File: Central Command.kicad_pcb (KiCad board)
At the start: 4 copper layers, 50.8 x 50.8 mm, 54 parts, among them P101 CONN_01X10, P102 CONN_01X10, P103 CONN_01X04, P104 CONN_01X02, P105 CONN_01X04, P106 CONN_01X02, P201 CONN_01X06, P202 CONN_01X04, P203 CONN_01X04, P204 CONN_01X03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

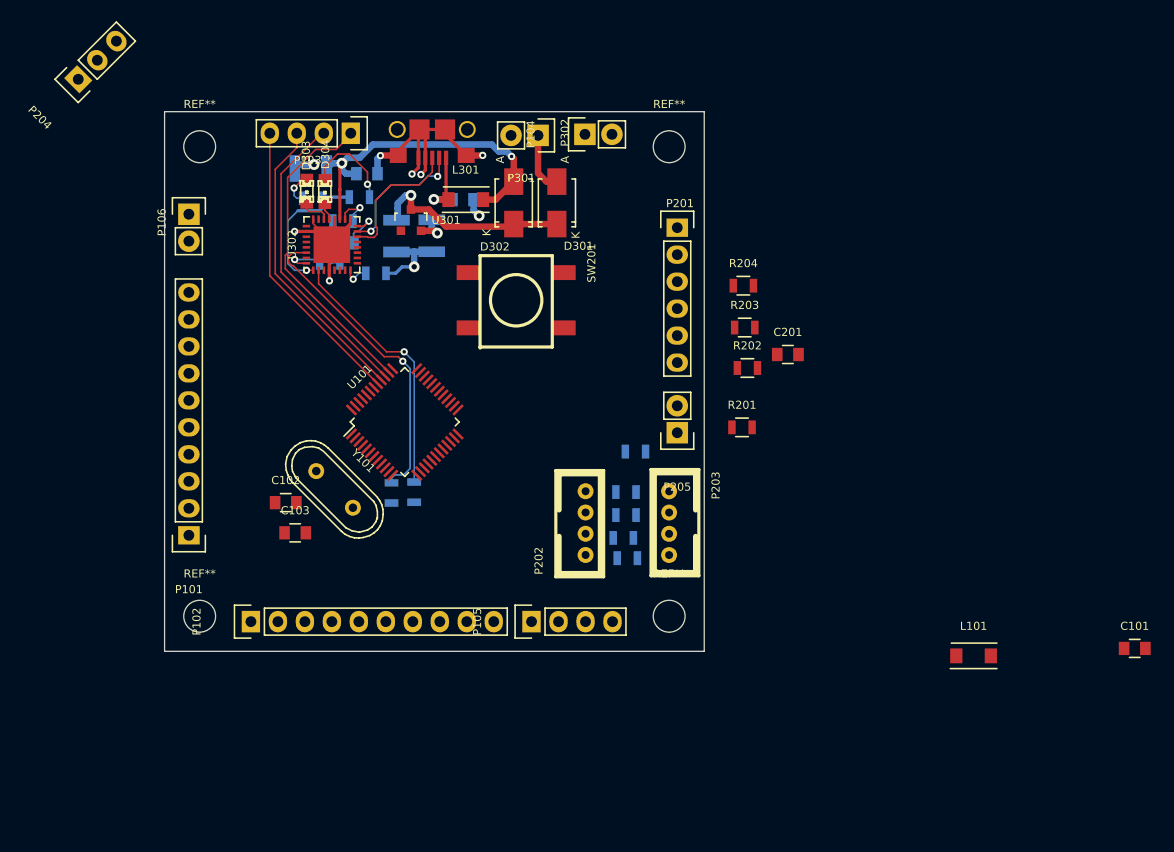
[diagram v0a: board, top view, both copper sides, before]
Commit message: Swapped two connectors and routed the bottom connector
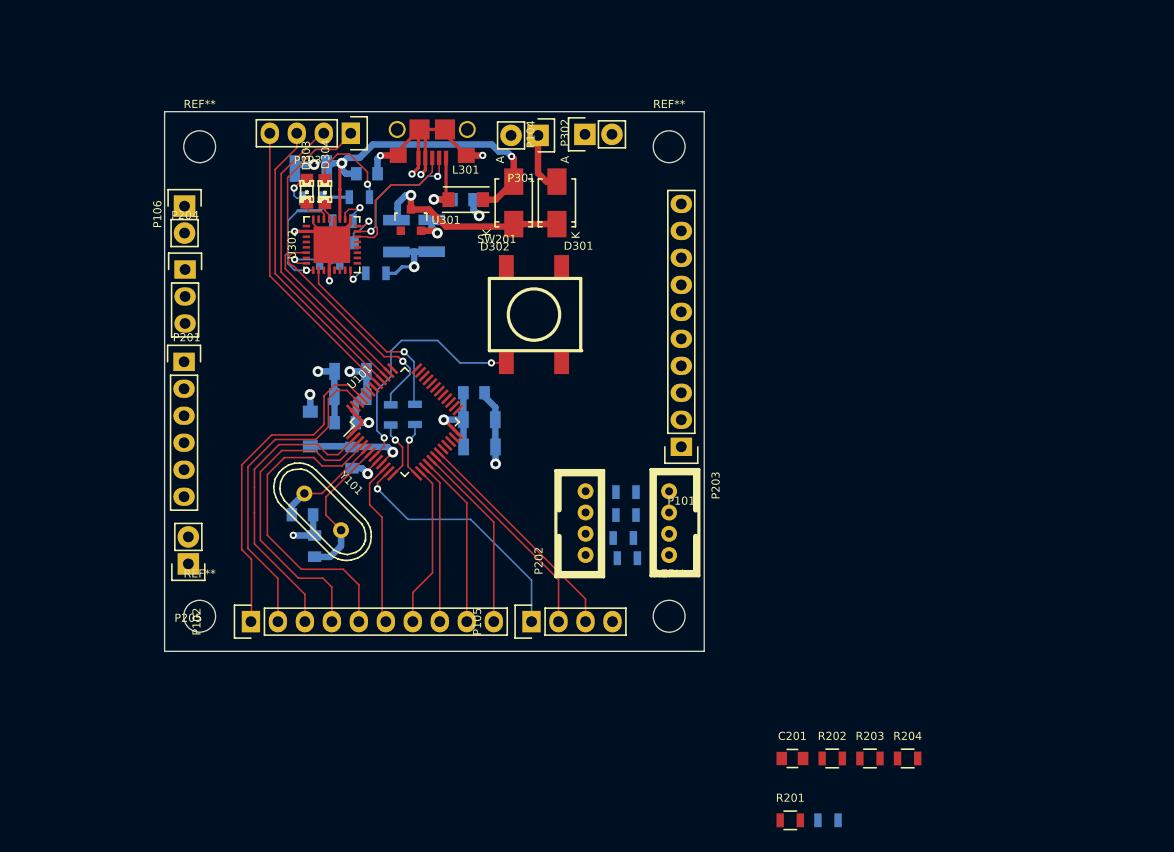
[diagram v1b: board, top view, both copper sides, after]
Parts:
- added C104: .1U, Capacitors_SMD:C_0805, B.Cu at (130.7, 102.7)
- added C105: 1U, Capacitors_SMD:C_1206, B.Cu at (131.3, 107.8)
- added C106: 10U, Capacitors_SMD:C_1206, B.Cu at (131.2, 105.2)
- added C107: .1U, Capacitors_SMD:C_0805, B.Cu at (118.6, 105.5)
- added C108: 1U, Capacitors_SMD:C_1206, B.Cu at (119.1, 103.0)
- added C109: 10U, Capacitors_SMD:C_1206, B.Cu at (119.1, 100.6)
- C101, C102, C103, L101: moved to B.Cu
- moved C101 75.9 mm to (119.2, 108.8), turned to 270 degrees
- moved L101 66.0 mm to (115.3, 106.1), turned to 270 degrees
- moved P201 48.1 mm to (103.4, 99.7)
- moved P205 47.7 mm to (103.8, 118.8)
- moved R204 47.1 mm to (171.5, 137.1)
- moved P101 47.1 mm to (150.2, 107.7)
- moved R203 42.2 mm to (168.0, 137.1)
- moved R205 39.2 mm to (164.0, 142.9)
- moved C201 38.0 mm to (160.7, 137.1)
- moved R202 37.6 mm to (164.4, 137.1)
- moved R201 37.3 mm to (160.5, 142.9)
- moved P204 20.5 mm to (103.5, 91.1), turned to 0 degrees
- moved R302 7.34 mm to (122.9, 104.7)
- moved R303 7.32 mm to (125.2, 104.7)
- moved Y101 2.39 mm to (116.5, 113.9)
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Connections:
- net Net-(C101-Pad1) renamed /VDDA
- P101 pad 10: Net-(P101-Pad10) -> /PA10
- P101 pad 8: Net-(P101-Pad8) -> /Comm/MCO
- P101 pad 9: Net-(P101-Pad9) -> /PA9
- P102 pad 1: Net-(P102-Pad1) -> /PB8
- P102 pad 2: Net-(P102-Pad2) -> /PB9
- P102 pad 4: /PB9 -> Net-(P102-Pad4)
- P102 pad 5: /Comm/MCO -> Net-(P102-Pad5)
- U101 pad 2: Net-(P102-Pad1) -> Net-(P102-Pad3)
- U101 pad 20: Net-(P101-Pad3) -> Net-(P101-Pad1)
- U101 pad 21: Net-(P101-Pad5) -> Net-(P101-Pad2)
- U101 pad 22: Net-(P101-Pad6) -> Net-(P101-Pad3)
- U101 pad 25: Net-(P101-Pad7) -> Net-(P101-Pad4)
- U101 pad 26: Net-(P101-Pad8) -> Net-(P101-Pad5)
- U101 pad 27: Net-(P101-Pad9) -> Net-(P101-Pad6)
- U101 pad 28: Net-(P101-Pad10) -> Net-(P101-Pad7)
- U101 pad 3: Net-(P102-Pad2) -> Net-(P102-Pad4)
- U101 pad 30: Net-(P101-Pad1) -> /PA9
- U101 pad 31: Net-(P101-Pad2) -> /PA10
- U101 pad 4: Net-(P102-Pad3) -> Net-(P102-Pad5)
- U101 pad 45: Net-(P101-Pad4) -> /PB8
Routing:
- net /PB8: track 0.00 -> 31.8 mm
- net /PB9: track 0.00 -> 31.2 mm
- net Net-(P102-Pad5): track 0.00 -> 30.5 mm
- net Net-(P102-Pad4): track 0.00 -> 29.5 mm
- net Net-(P102-Pad3): track 0.00 -> 27.8 mm
- net /ADC_IN1: track 0.00 -> 24.0 mm, vias 0 -> 1
- net /Comm/NRST: track 0.00 -> 23.3 mm, vias 0 -> 2
- net /Comm/PWR: track 3.10 -> 26.3 mm, vias 1 -> 5
- net /ADC_IN9: track 0.00 -> 21.6 mm
- net GND: track 57.3 -> 78.3 mm, vias 9 -> 13
- net /ADC_IN8: track 0.00 -> 20.3 mm
- net Net-(P102-Pad10): track 0.00 -> 17.6 mm
- net Net-(P102-Pad9): track 0.00 -> 16.3 mm
- net Net-(P102-Pad6): track 0.00 -> 15.7 mm
- net Net-(P102-Pad7): track 0.00 -> 15.4 mm
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
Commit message: Removed one header and finished connecting all parts
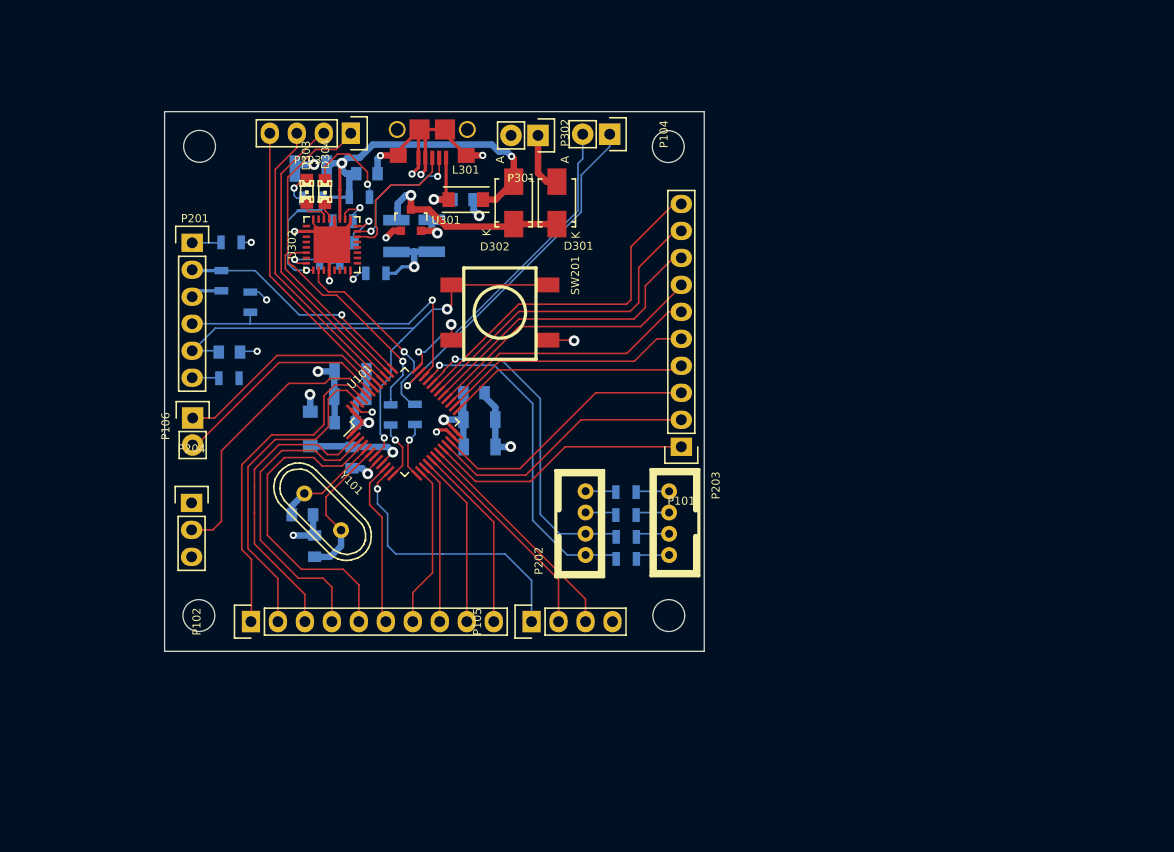
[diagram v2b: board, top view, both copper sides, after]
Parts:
- removed P205: CONN_01X02, Pin_Headers:Pin_Header_Straight_1x02
- removed R205: R, Resistors_SMD:R_0805
- removed the REF** at (149.1, 123.7)
- removed the REF** at (104.9, 123.7)
- removed the REF** at (149.1, 79.5)
- removed the REF** at (104.9, 79.5)
- added REF**: MountingHole_3mm, Mounting_Holes:MountingHole_3mm, F.Cu at (149.0, 79.5)
- added REF**: MountingHole_3mm, Mounting_Holes:MountingHole_3mm, F.Cu at (149.1, 123.6)
- added REF**: MountingHole_3mm, Mounting_Holes:MountingHole_3mm, F.Cu at (104.8, 123.6)
- added REF**: MountingHole_3mm, Mounting_Holes:MountingHole_3mm, F.Cu at (104.9, 79.5)
- C201, R201, R202, R203, R204: moved to B.Cu
- moved R203 77.3 mm to (107.9, 88.5), turned to 180 degrees
- moved R201 73.8 mm to (107.0, 92.1), turned to 270 degrees
- moved R204 73.2 mm to (107.7, 101.3)
- moved R202 69.6 mm to (109.7, 94.1), turned to 270 degrees
- moved C201 65.4 mm to (107.7, 98.8)
- moved P204 22.0 mm to (104.1, 113.0)
- moved P106 20.0 mm to (104.2, 105.0)
- moved P201 11.2 mm to (104.2, 88.5)
- moved SW201 3.22 mm to (133.2, 95.1), turned to 90 degrees
- moved P104 2.33 mm to (143.5, 78.3), turned to 270 degrees
- moved R208 0.30 mm to (145.1, 116.2)
- moved R209 0.12 mm to (145.1, 118.3)
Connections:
- net /Comm/MCO renamed /MCO
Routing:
- net /I2C1_SDA: track 0.00 -> 33.3 mm, vias 0 -> 1
- net /PA10: track 0.00 -> 33.2 mm
- net /Comm/SDA: track 0.00 -> 32.5 mm, vias 0 -> 1
- net /Comm/SWIO: track 0.00 -> 32.2 mm, vias 0 -> 1
- net /Comm/SCL: track 0.00 -> 31.7 mm, vias 0 -> 1
- net /PA9: track 0.00 -> 31.0 mm
- net /Comm/NRST: track 23.3 -> 53.7 mm
- net /I2C1_SCL: track 0.00 -> 29.9 mm, vias 0 -> 1
- net /MCO: track 0.00 -> 29.0 mm
- net /Comm/BOOT0: track 0.00 -> 26.9 mm
- net Net-(P101-Pad7): track 0.00 -> 26.6 mm
- net Net-(P101-Pad3): track 0.00 -> 25.7 mm
- net Net-(P101-Pad2): track 0.00 -> 25.4 mm
- net Net-(P101-Pad6): track 0.00 -> 25.3 mm
- net Net-(P101-Pad1): track 0.00 -> 25.0 mm
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
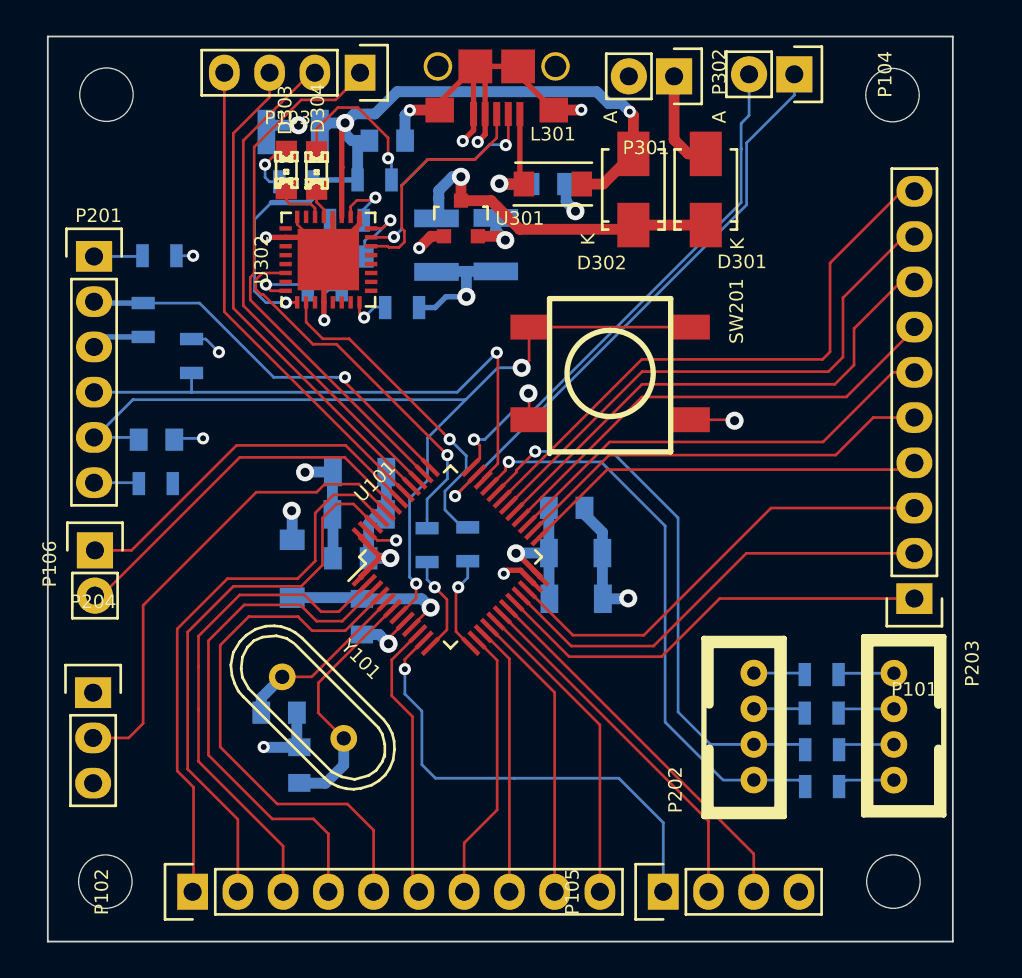
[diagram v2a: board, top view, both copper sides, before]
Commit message: Finished layout including labels and DRC
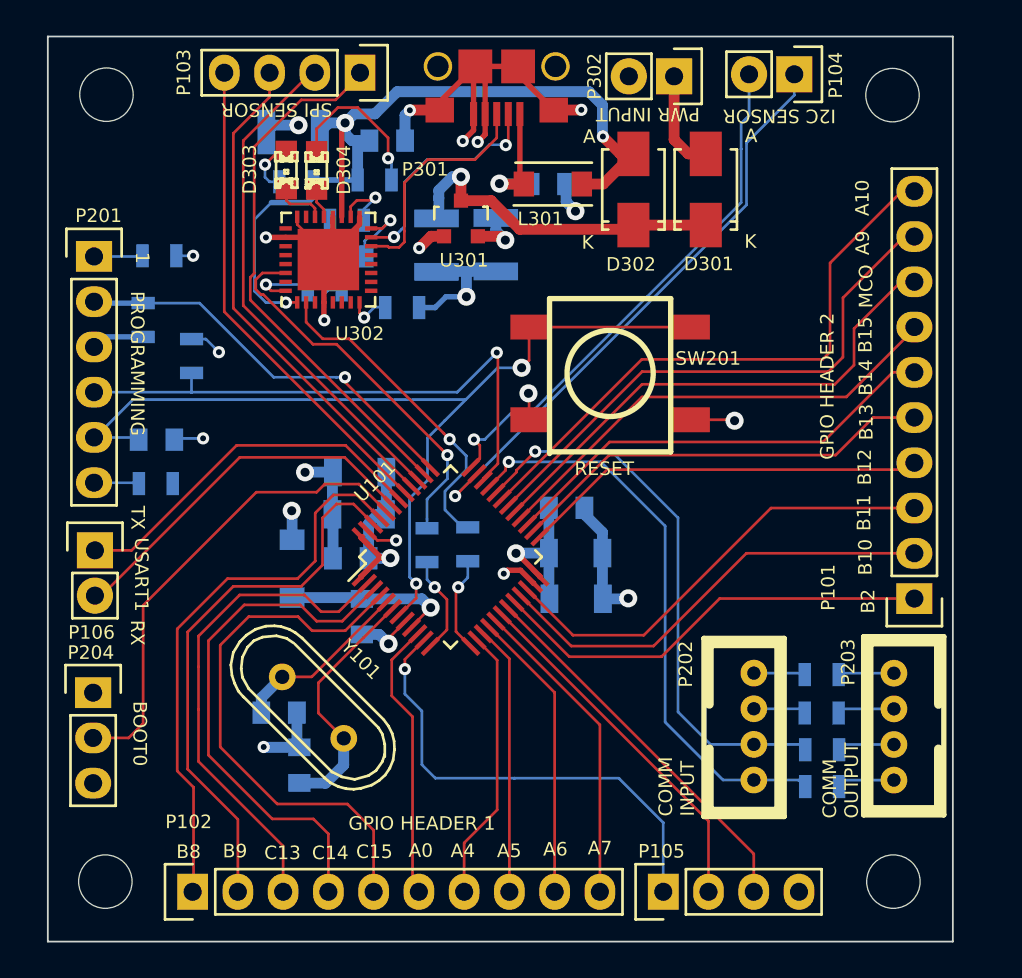
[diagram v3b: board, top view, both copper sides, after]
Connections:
- net Net-(P101-Pad1) renamed /PB2
- net Net-(P101-Pad2) renamed /PB10
- net Net-(P101-Pad3) renamed /PB11
- net Net-(P101-Pad4) renamed /PB12
- net Net-(P101-Pad5) renamed /PB13
- net Net-(P101-Pad6) renamed /PB14
- net Net-(P101-Pad7) renamed /PB15
- net Net-(P102-Pad10) renamed /PA7
- net Net-(P102-Pad3) renamed /PC13
- net Net-(P102-Pad4) renamed /PC14
- net Net-(P102-Pad5) renamed /PC15
- net Net-(P102-Pad6) renamed /PA0
- net Net-(P102-Pad7) renamed /PA4
- net Net-(P102-Pad8) renamed /PA5
- net Net-(P102-Pad9) renamed /PA6
- P301 pad 6: (no net) -> GND
- P301 pad 7: (no net) -> GND
- P301 pad 8: (no net) -> GND
- P301 pad 9: (no net) -> GND
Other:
- board text added: "1"
- board text added: "A0"
- board text added: "A10"
- board text added: "A4"
- board text added: "A5"
- board text added: "A6"
- board text added: "A7"
- board text added: "A9"
- board text added: "B10"
- board text added: "B11"
- board text added: "B12"
- board text added: "B13"
- board text added: "B14"
- board text added: "B15"
- board text added: "B2"
- board text added: "B8"
- board text added: "B9"
- board text added: "BOOT0"
- board text added: "C13"
- board text added: "C14"
- board text added: "C15"
- board text added: "COMM INPUT"
- board text added: "COMM OUTPUT"
- board text added: "GPIO HEADER 1"
- board text added: "GPIO HEADER 2"
- board text added: "I2C SENSOR"
- board text added: "MCO"
- board text added: "PROGRAMMING"
- board text added: "PWR INPUT"
- board text added: "RESET"
- board text added: "RX"
- board text added: "SPI SENSOR"
- board text added: "TX"
- board text added: "USART1"

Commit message: Finished board and generated gerbers
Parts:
- added G***: LOGO, CentralCommand:CClogo-small, B.Cu at (138.3, 91.4)
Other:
- board text added: "Central Command Rev 1"
- board text added: "MISO"
- board text added: "MOSI"
